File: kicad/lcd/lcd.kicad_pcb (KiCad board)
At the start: 2 copper layers, 145.4 x 93.8 mm, 31 parts, among them J1 Screw_Terminal_01x02, J2 Screw_Terminal_01x02, Q1 NPN, Q2 PNP, Q3 NPN, SW1 RotaryEncoder_Switch, U3 LM7805_TO220

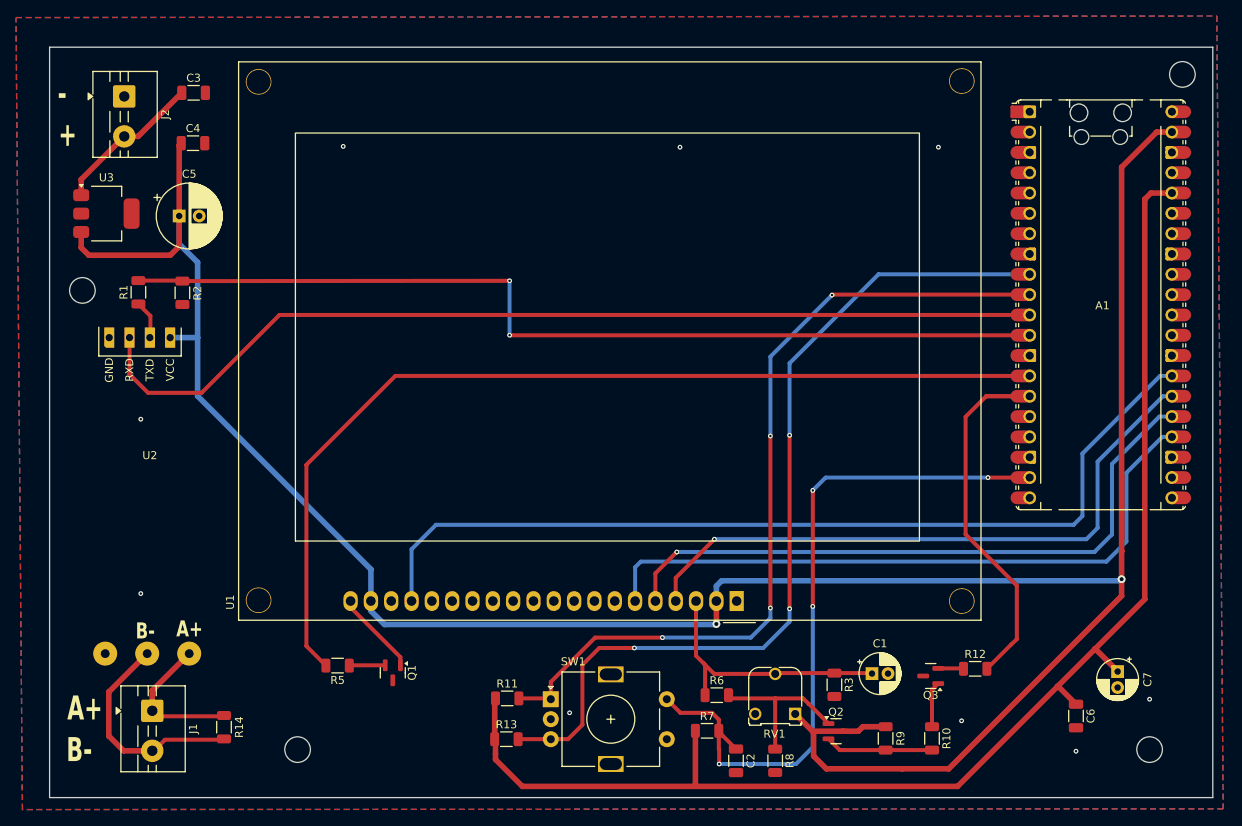
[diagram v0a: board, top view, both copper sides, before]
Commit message: change mounting holes
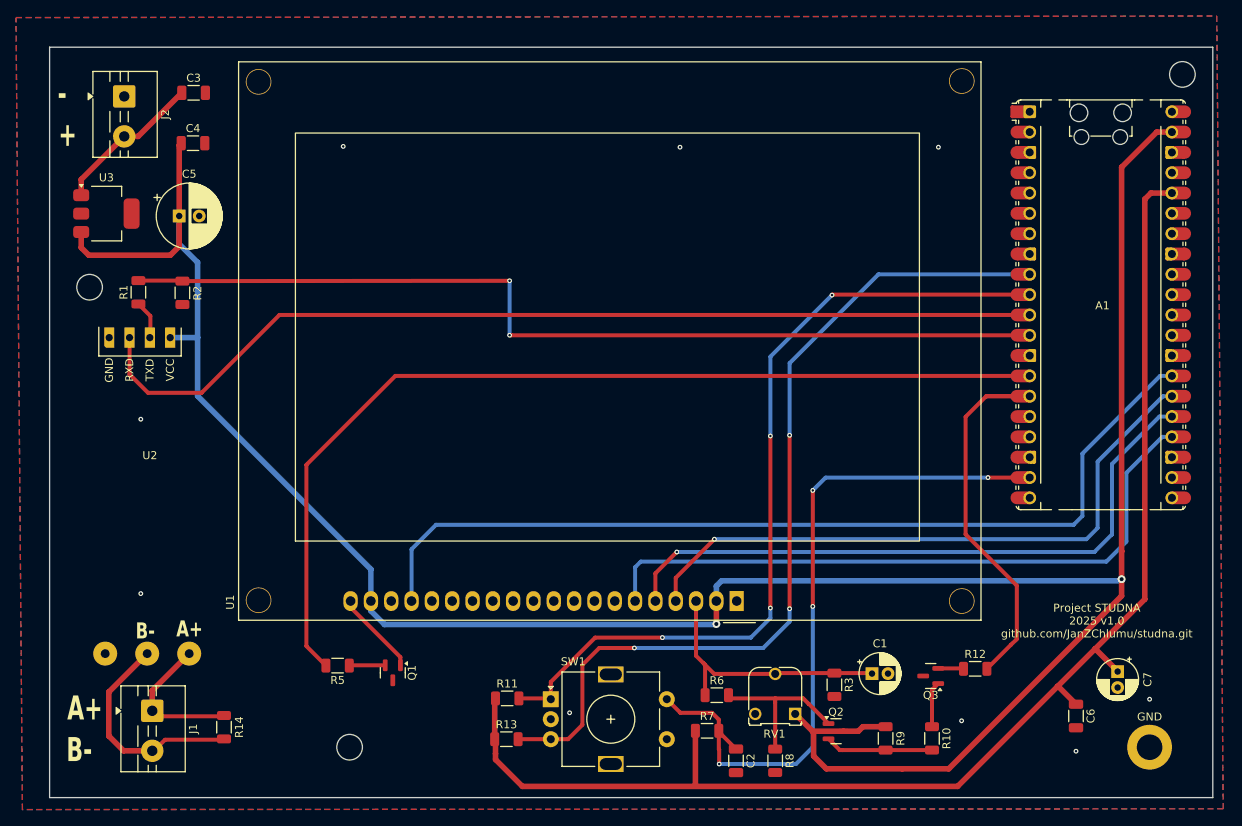
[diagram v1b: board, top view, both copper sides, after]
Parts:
- added GND: MountingHole_3.2mm_M3_DIN965_Pad, MountingHole:MountingHole_3.2mm_M3_DIN965_Pad, F.Cu at (211.1, 141.2)
- added REF**: MountingHole_3.2mm_M3_ISO7380, MountingHole:MountingHole_3.2mm_M3_ISO7380, F.Cu at (111.0, 141.2)
- added REF**: MountingHole_3.2mm_M3_ISO7380, MountingHole:MountingHole_3.2mm_M3_ISO7380, F.Cu at (78.5, 83.8)
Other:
- outline, holes or cut-outs redrawn
- board text added: "Project STUDNA 2025 v1.0 github.com/JanZChlumu/studna.git"

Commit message: pcb ramecek potenciometru
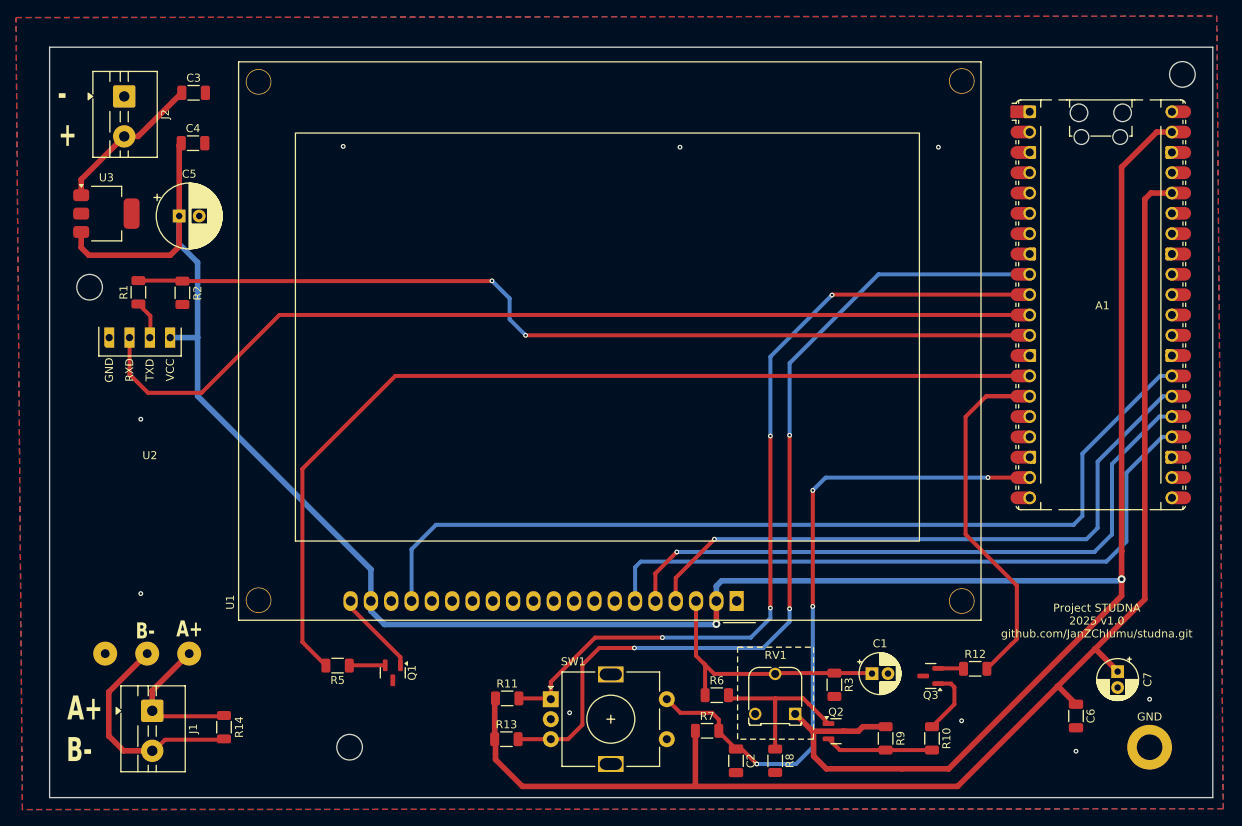
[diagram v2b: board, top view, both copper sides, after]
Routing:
- net /button: track 88.7 -> 82.4 mm
- net Net-(Q3-C): track 5.71 -> 8.31 mm
- net /UART1_RX: track 118.2 -> 115.8 mm
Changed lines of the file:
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@@
 		(tags "Potentiometer Trimmer RM-065")
 		(property "Reference" "RV1"
-			(at 2.6 -2.5 0)
+			(at 2.45 7.34 0)
 			(layer "F.SilkS")
 			(effects
@@
 		)
 	)
+	(gr_rect
+		(start 159.55 128.75)
+		(end 169.05 140.25)
+		(stroke
+			(width 0.1)
+			(type dash)
+		)
+		(fill no)
+		(layer "F.SilkS")
+	)
 	(gr_circle
 		(center 215.15 57.15)
@@
 	)
 	(segment
-		(start 157.25 143.35)
-		(end 157.25 141.55)
-		(width 0.5)
-		(layer "F.Cu")
-		(net 1)
-	)
-	(segment
 		(start 152.4 136.95)
 		(end 150.7 135.25)
@@
 	)
 	(segment
-		(start 157.25 141.55)
-		(end 157.2 141.5)
-		(width 0.5)
-		(layer "F.Cu")
-		(net 1)
-	)
-	(segment
 		(start 196.06 107.54)
 		(end 190.86 107.54)
@@
 	)
 	(segment
-		(start 157.2 141.5)
-		(end 157.2 139.2)
-		(width 0.5)
-		(layer "F.Cu")
-		(net 1)
-	)
-	(segment
 		(start 156.35 136.95)
 		(end 152.4 136.95)
+		(width 0.5)
+		(layer "F.Cu")
+		(net 1)
+	)
+	(segment
+		(start 161.95 143.35)
+		(end 160.15 141.55)
 		(width 0.5)
 		(layer "F.Cu")
@@
 	)
 	(via
-		(at 157.25 143.35)
+		(at 161.95 143.35)
 		(size 0.6)
 		(drill 0.3)
@@
 	)
 	(segment
+		(start 161.95 143.35)
+		(end 166.85 143.35)
+		(width 0.5)
+		(layer "B.Cu")
+		(net 1)
+	)
+	(segment
+		(start 166.85 143.35)
+		(end 168.95 141.25)
+		(width 0.5)
+		(layer "B.Cu")
+		(net 1)
+	)
+	(segment
+		(start 170.55 107.55)
+		(end 168.95 109.15)
+		(width 0.5)
+		(layer "B.Cu")
+		(net 1)
+	)
+	(segment
 		(start 168.95 141.25)
 		(end 168.95 123.65)
@@
 	)
 	(segment
-		(start 157.25 143.35)
-		(end 166.85 143.35)
-		(width 0.5)
-		(layer "B.Cu")
-		(net 1)
-	)
-	(segment
-		(start 170.55 107.55)
-		(end 168.95 109.15)
-		(width 0.5)
-		(layer "B.Cu")
-		(net 1)
-	)
-	(segment
-		(start 166.85 143.35)
-		(end 168.95 141.25)
-		(width 0.5)
-		(layer "B.Cu")
-		(net 1)
+		(start 133.05 89.76)
+		(end 196.06 89.76)
+		(width 0.5)
+		(layer "F.Cu")
+		(net 2)
 	)
 	(segment
@@
 	)
 	(segment
-		(start 131.24 89.76)
-		(end 196.06 89.76)
+		(start 128.85 82.952017)
+		(end 128.814517 82.9875)
 		(width 0.5)
 		(layer "F.Cu")
@@
 	)
 	(segment
-		(start 131.23 89.75)
-		(end 131.24 89.76)
-		(width 0.5)
-		(layer "F.Cu")
-		(net 2)
-	)
-	(segment
-		(start 131.05 89.75)
-		(end 131.23 89.75)
-		(width 0.5)
-		(layer "F.Cu")
-		(net 2)
-	)
-	(segment
-		(start 131.05 82.95)
+		(start 128.814517 82.9875)
 		(end 90.15 82.9875)
 		(width 0.5)
@@
 	)
 	(via
-		(at 131.05 82.95)
+		(at 128.85 82.952017)
 		(size 0.6)
 		(drill 0.3)
@@
 	)
 	(via
-		(at 131.05 89.75)
+		(at 133.05 89.76)
 		(size 0.6)
 		(drill 0.3)
@@
 	)
 	(segment
-		(start 131.05 89.75)
-		(end 131.05 82.95)
+		(start 131.05 87.76)
+		(end 131.05 85.152017)
+		(width 0.5)
+		(layer "B.Cu")
+		(net 2)
+	)
+	(segment
+		(start 131.05 85.152017)
+		(end 128.85 82.952017)
+		(width 0.5)
+		(layer "B.Cu")
+		(net 2)
+	)
+	(segment
+		(start 133.05 89.76)
+		(end 131.05 87.76)
 		(width 0.5)
 		(layer "B.Cu")
@@
 	(segment
 		(start 108.0875 131.05)
-		(end 105.65 128.6125)
+		(end 105.15 128.1125)
 		(width 0.5)
 		(layer "F.Cu")
@@
 	)
 	(segment
-		(start 105.65 105.95)
-		(end 116.76 94.84)
+		(start 105.15 128.1125)
+		(end 105.15 106.45)
 		(width 0.5)
 		(layer "F.Cu")
@@
 	)
 	(segment
-		(start 105.65 128.6125)
-		(end 105.65 105.95)
-		(width 0.5)
-		(layer "F.Cu")
-		(net 29)
-	)
-	(segment
 		(start 195.26 94.84)
 		(end 196.06 94.84)
+		(width 0.5)
+		(layer "F.Cu")
+		(net 29)
+	)
+	(segment
+		(start 105.15 106.45)
+		(end 116.76 94.84)
 		(width 0.5)
 		(layer "F.Cu")
@@
 	)
 	(segment
+		(start 186.65 133.75)
+		(end 186.65 135.8875)
+		(width 0.5)
+		(layer "F.Cu")
+		(net 56)
+	)
+	(segment
+		(start 186.2 133.3)
+		(end 186.65 133.75)
+		(width 0.5)
+		(layer "F.Cu")
+		(net 56)
+	)
+	(segment
+		(start 186.65 135.8875)
+		(end 183.85 138.6875)
+		(width 0.5)
+		(layer "F.Cu")
+		(net 56)
+	)
+	(segment
 		(start 184.625 133.3)
-		(end 183.85 134.075)
-		(width 0.5)
-		(layer "F.Cu")
-		(net 56)
-	)
-	(segment
-		(start 183.85 134.075)
-		(end 183.85 138.6875)
-		(width 0.5)
-		(layer "F.Cu")
+		(end 186.2 133.3)
+		(width 0.5)
+		(layer "F.Cu")
